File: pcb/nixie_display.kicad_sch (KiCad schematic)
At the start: 12 parts, among them U1 IC_SR_MC_HV5622PG-G, U2 IC_SR_MC_HV5622PG-G

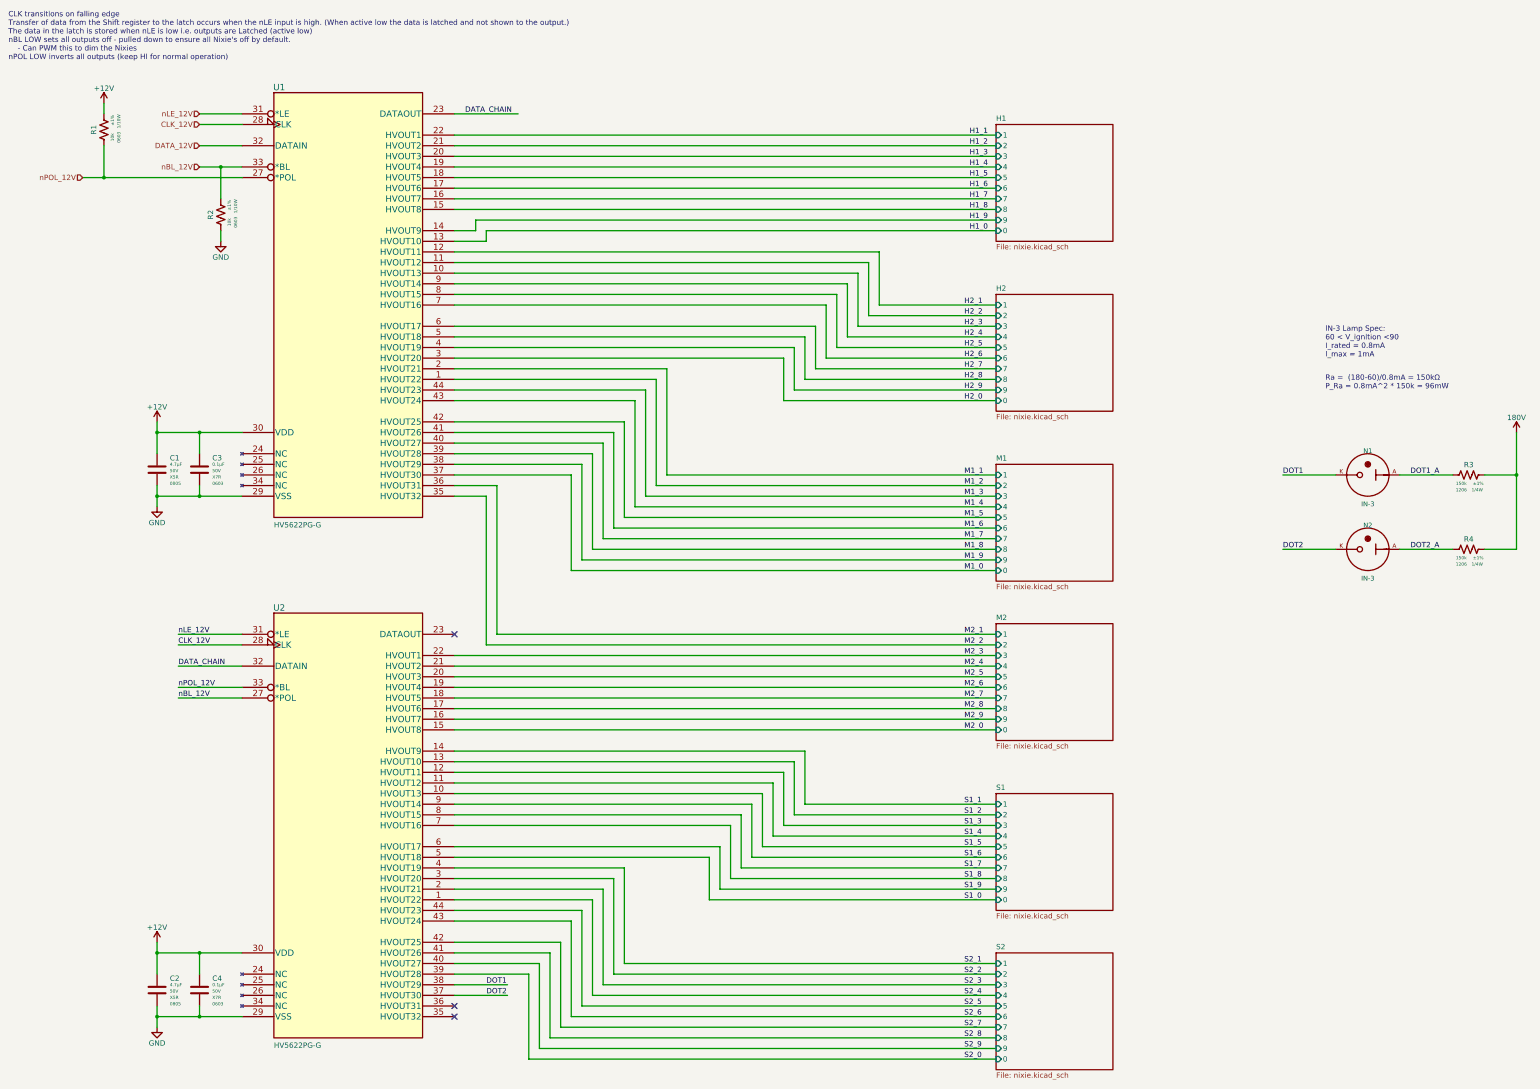
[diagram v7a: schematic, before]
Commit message: Reshuffled nixie schematic to ease with routing. Need to fix the other 3 digits next.
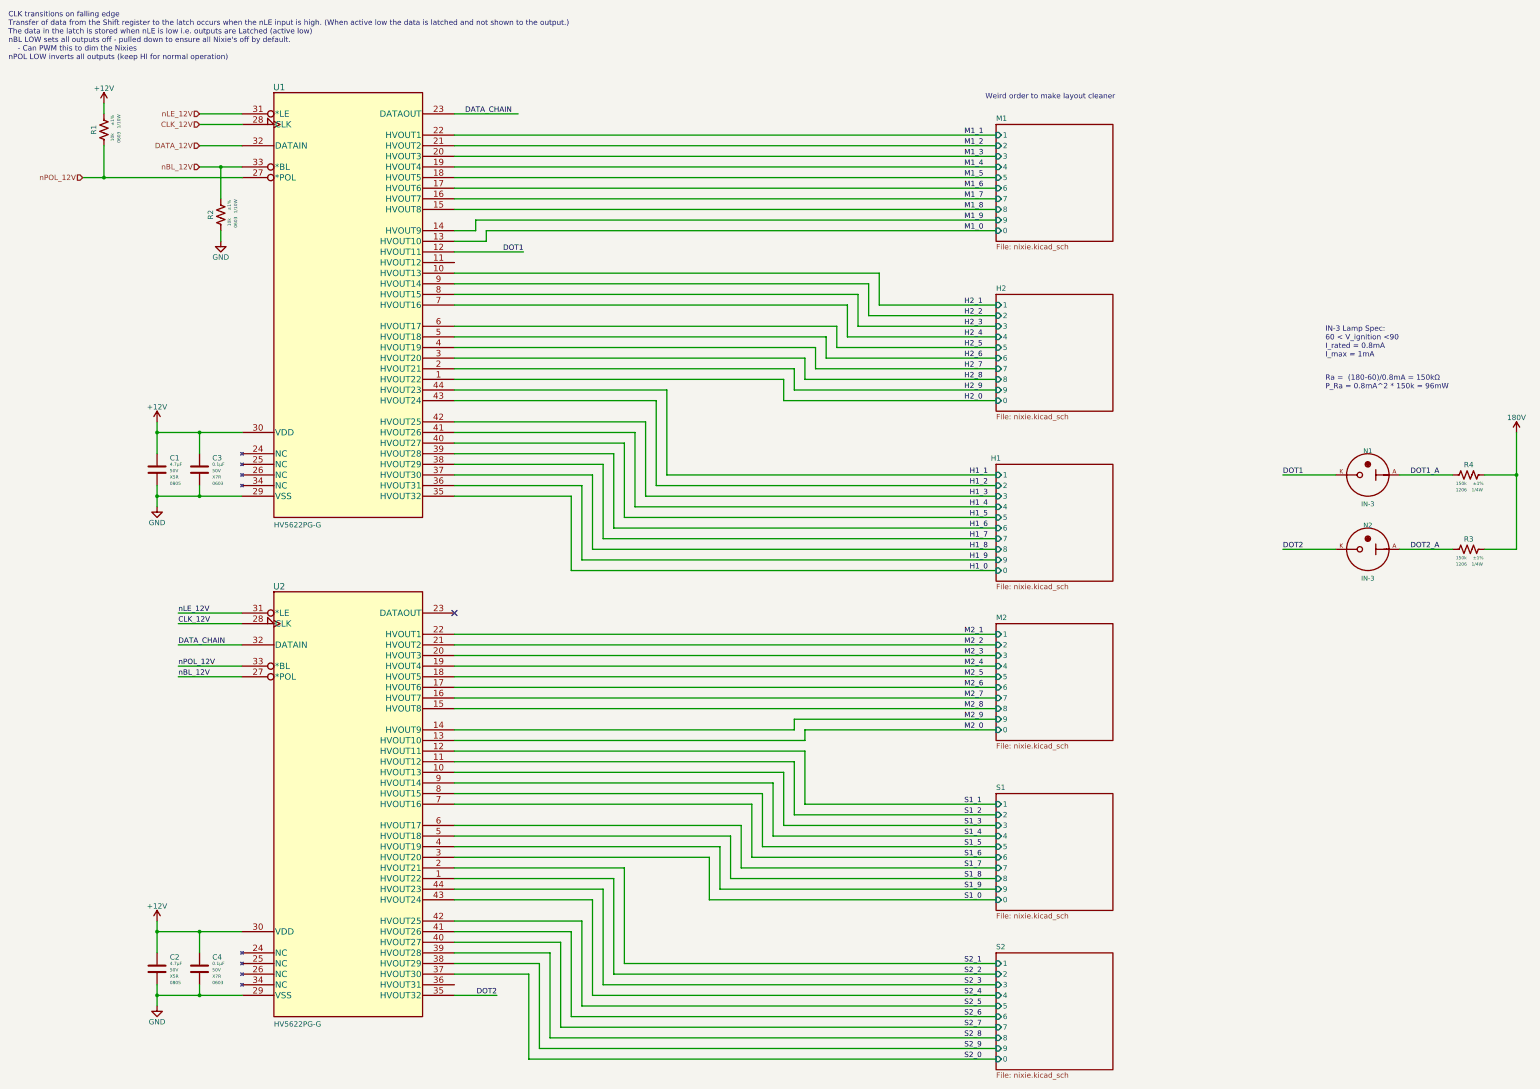
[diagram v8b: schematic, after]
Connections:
- net DOT1: now also U1.12 (HVOUT11); no longer U2.38 (HVOUT29)
- net DOT1_A: now also R4.2; no longer R3.2
- net DOT2: now also U2.35 (HVOUT32); no longer U2.37 (HVOUT30)
- net DOT2_A: now also R3.2; no longer R4.2
- net H1_0: now also U1.35 (HVOUT32); no longer U1.13 (HVOUT10)
- net H1_1: now also U1.44 (HVOUT23); no longer U1.22 (HVOUT1)
- net H1_2: now also U1.43 (HVOUT24); no longer U1.21 (HVOUT2)
- net H1_3: now also U1.42 (HVOUT25); no longer U1.20 (HVOUT3)
- net H1_4: now also U1.41 (HVOUT26); no longer U1.19 (HVOUT4)
- net H1_5: now also U1.40 (HVOUT27); no longer U1.18 (HVOUT5)
- net H1_6: now also U1.39 (HVOUT28); no longer U1.17 (HVOUT6)
- net H1_7: now also U1.38 (HVOUT29); no longer U1.16 (HVOUT7)
- net H1_8: now also U1.37 (HVOUT30); no longer U1.15 (HVOUT8)
- net H1_9: now also U1.36 (HVOUT31); no longer U1.14 (HVOUT9)
- net H2_0: now also U1.1 (HVOUT22); no longer U1.3 (HVOUT20)
- net H2_1: now also U1.10 (HVOUT13); no longer U1.12 (HVOUT11)
- net H2_2: now also U1.9 (HVOUT14); no longer U1.11 (HVOUT12)
- net H2_3: now also U1.8 (HVOUT15); no longer U1.10 (HVOUT13)
- net H2_4: now also U1.7 (HVOUT16); no longer U1.9 (HVOUT14)
- net H2_5: now also U1.6 (HVOUT17); no longer U1.8 (HVOUT15)
- net H2_6: now also U1.5 (HVOUT18); no longer U1.7 (HVOUT16)
- net H2_7: now also U1.4 (HVOUT19); no longer U1.6 (HVOUT17)
- net H2_8: now also U1.3 (HVOUT20); no longer U1.5 (HVOUT18)
- net H2_9: now also U1.2 (HVOUT21); no longer U1.4 (HVOUT19)
- net M1_0: now also U1.13 (HVOUT10); no longer U1.37 (HVOUT30)
- net M1_1: now also U1.22 (HVOUT1); no longer U1.2 (HVOUT21)
- net M1_2: now also U1.21 (HVOUT2); no longer U1.1 (HVOUT22)
- net M1_3: now also U1.20 (HVOUT3); no longer U1.44 (HVOUT23)
- net M1_4: now also U1.19 (HVOUT4); no longer U1.43 (HVOUT24)
- net M1_5: now also U1.18 (HVOUT5); no longer U1.42 (HVOUT25)
- net M1_6: now also U1.17 (HVOUT6); no longer U1.41 (HVOUT26)
- net M1_7: now also U1.16 (HVOUT7); no longer U1.40 (HVOUT27)
- net M1_8: now also U1.15 (HVOUT8); no longer U1.39 (HVOUT28)
- net M1_9: now also U1.14 (HVOUT9); no longer U1.38 (HVOUT29)
- net M2_0: now also U2.13 (HVOUT10); no longer U2.15 (HVOUT8)
- net M2_1: now also U2.22 (HVOUT1); no longer U1.36 (HVOUT31)
- net M2_2: now also U2.21 (HVOUT2); no longer U1.35 (HVOUT32)
- net M2_3: now also U2.20 (HVOUT3); no longer U2.22 (HVOUT1)
- net M2_4: now also U2.19 (HVOUT4); no longer U2.21 (HVOUT2)
- net M2_5: now also U2.18 (HVOUT5); no longer U2.20 (HVOUT3)
- net M2_6: now also U2.17 (HVOUT6); no longer U2.19 (HVOUT4)
- net M2_7: now also U2.16 (HVOUT7); no longer U2.18 (HVOUT5)
- net M2_8: now also U2.15 (HVOUT8); no longer U2.17 (HVOUT6)
- net M2_9: now also U2.14 (HVOUT9); no longer U2.16 (HVOUT7)
- net S1_0: now also U2.3 (HVOUT20); no longer U2.5 (HVOUT18)
- net S1_1: now also U2.12 (HVOUT11); no longer U2.14 (HVOUT9)
- net S1_2: now also U2.11 (HVOUT12); no longer U2.13 (HVOUT10)
- net S1_3: now also U2.10 (HVOUT13); no longer U2.12 (HVOUT11)
- net S1_4: now also U2.9 (HVOUT14); no longer U2.11 (HVOUT12)
- net S1_5: now also U2.8 (HVOUT15); no longer U2.10 (HVOUT13)
- net S1_6: now also U2.7 (HVOUT16); no longer U2.9 (HVOUT14)
- net S1_7: now also U2.6 (HVOUT17); no longer U2.8 (HVOUT15)
- net S1_8: now also U2.5 (HVOUT18); no longer U2.7 (HVOUT16)
- net S1_9: now also U2.4 (HVOUT19); no longer U2.6 (HVOUT17)
- net S2_0: now also U2.37 (HVOUT30); no longer U2.39 (HVOUT28)
- net S2_1: now also U2.2 (HVOUT21); no longer U2.4 (HVOUT19)
- net S2_2: now also U2.1 (HVOUT22); no longer U2.3 (HVOUT20)
- net S2_3: now also U2.44 (HVOUT23); no longer U2.2 (HVOUT21)
- net S2_4: now also U2.43 (HVOUT24); no longer U2.1 (HVOUT22)
- net S2_5: now also U2.42 (HVOUT25); no longer U2.44 (HVOUT23)
- net S2_6: now also U2.41 (HVOUT26); no longer U2.43 (HVOUT24)
- net S2_7: now also U2.40 (HVOUT27); no longer U2.42 (HVOUT25)
- net S2_8: now also U2.39 (HVOUT28); no longer U2.41 (HVOUT26)
- net S2_9: now also U2.38 (HVOUT29); no longer U2.40 (HVOUT27)
- no-connect marks 3 -> 1
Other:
- note added: "Weird order to make layout cleaner"
